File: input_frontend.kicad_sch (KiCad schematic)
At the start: 15 parts

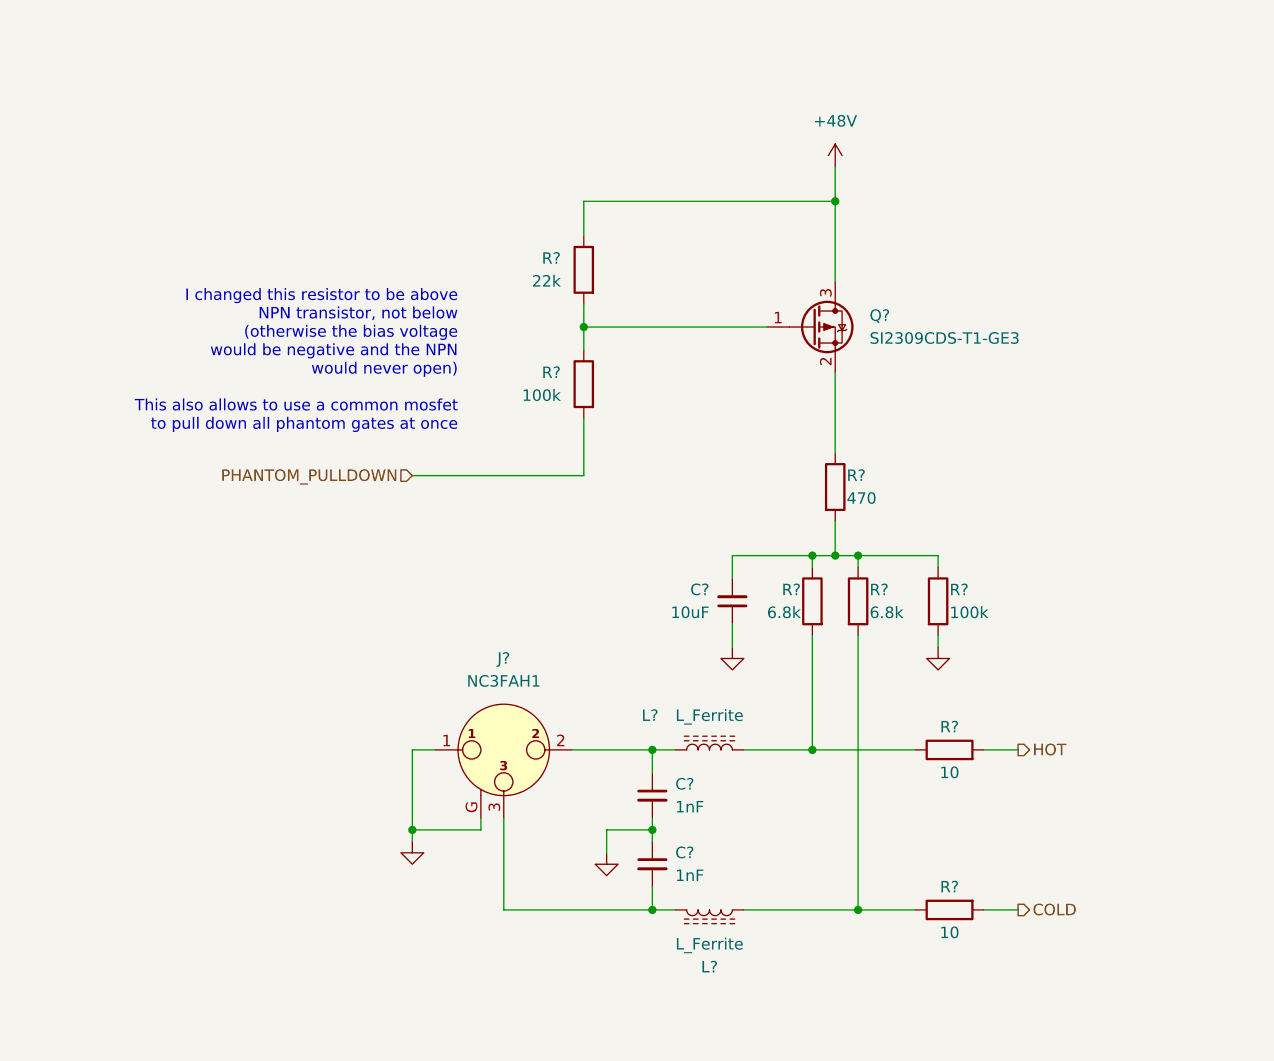
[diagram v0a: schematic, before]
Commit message: independent phantom control and removed transformer bias
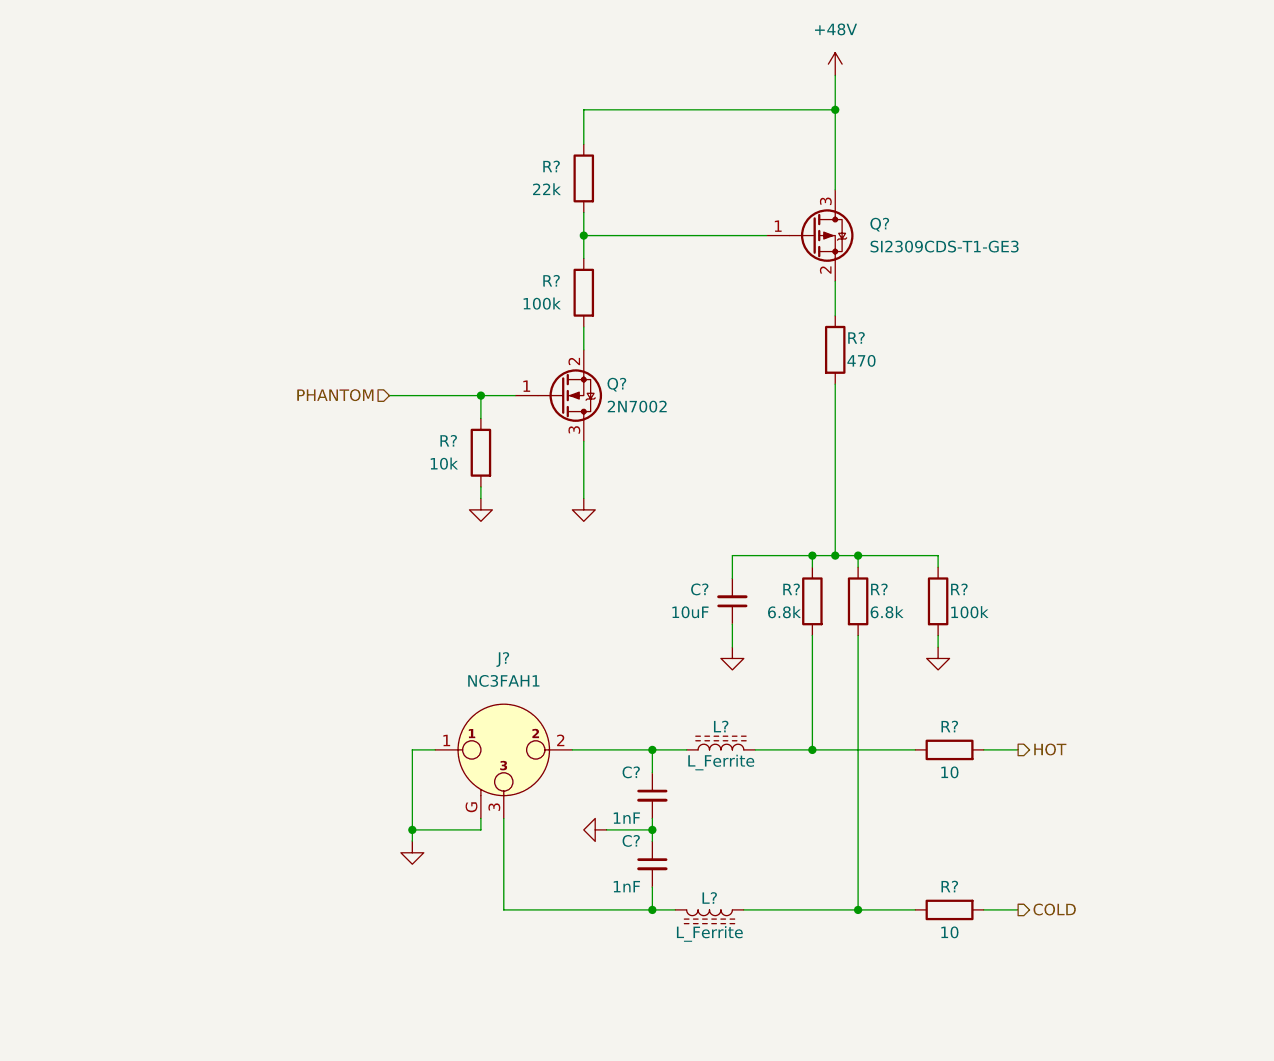
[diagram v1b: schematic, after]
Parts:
- added Q?: 2N7002, Package_TO_SOT_SMD:SOT-23, symbol Transistor_FET:2N7002
- added R?: 10k, Resistor_SMD:R_0603_1608Metric, symbol Device:R
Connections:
- net GND: now also Q?.3 (D), R?.2
- net PHANTOM_PULLDOWN: no longer names the net of R?.2
- net PHANTOM_PULLDOWN: now also Q?.2 (S)
- new net PHANTOM: Q?.1 (G), R?.1
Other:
- note removed: "I changed this resistor to be above NPN transistor, not below (otherwise the bias voltage would be negative and the NPN would never open) This also allows to use a common mosfet to pull down all phantom gates at once"
- moved on the sheet: L?, Q?, R?

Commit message: assign some component data
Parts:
- C16, C17: renamed from C?; value 1nF -> 1nF 63V; MPN (none) -> C 1nF 63V 0805
- C18: renamed from C?; MPN (none) -> C 10μF 16V 0805
- J2: renamed from J?; MPN (none) -> NC3FAH1
- L1, L2: renamed from L?; MPN (none) -> must select ferrite; now left out of the parts list
- Q1: renamed from Q?; MPN (none) -> 2N7002
- Q2: renamed from Q?; MPN (none) -> SI2309CDS-T1-GE3
- R10, R8: renamed from R?; MPN (none) -> R 6.8kΩ 125mW 1% 0805
- R11, R7: renamed from R?; MPN (none) -> R 100kΩ 125mW 5% 0805
- R12, R13: renamed from R?; MPN (none) -> R 10Ω 125mW 5% 0805
- R5: renamed from R?; MPN (none) -> R 10kΩ 125mW 5% 0805
- R6: renamed from R?; MPN (none) -> R 22kΩ 125mW 5% 0805
- R9: renamed from R?; MPN (none) -> R 470Ω 125mW 5% 0805

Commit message: some final touches
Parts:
- added R14: 13kΩ, Resistor_SMD:R_0603_1608Metric, symbol Device:R
- R10, R8: value 6.8k -> 6.8kΩ
- R11, R7: value 100k -> 100kΩ
- R12, R13: value 10 -> 2.2kΩ; MPN R 10Ω 125mW 5% 0805 -> R 2.2kΩ 125mW 1% 0805
- R5: value 10k -> 10kΩ
- R6: value 22k -> 22kΩ
- R9: value 470 -> 470Ω
- renumbered J2 to J1
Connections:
- net COLD: now also R14.2
- net HOT: now also R14.1
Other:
- note added: "replace with 10Ω and remove parallel resistor to disable pad"
- note added: "≈6dB pad with ≈10k impedance"

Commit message: update component assignments
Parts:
- C16, C17: MPN C 1nF 63V 0805 -> C 1nF 63V 0603
- C18: footprint Capacitor_SMD:C_0603_1608Metric -> Capacitor_SMD:C_0805_2012Metric
- R10, R8: MPN R 6.8kΩ 125mW 1% 0805 -> R 6.8kΩ 125mW 1% 0603
- R11, R7: MPN R 100kΩ 125mW 5% 0805 -> R 100kΩ 125mW 5% 0603
- R12, R13: MPN R 2.2kΩ 125mW 1% 0805 -> R 2.2kΩ 125mW 1% 0603
- R14: MPN R 13kΩ 125mW 1% 0805 -> R 13kΩ 125mW 1% 0603
- R5: MPN R 10kΩ 125mW 5% 0805 -> R 10kΩ 125mW 5% 0603
- R6: MPN R 22kΩ 125mW 5% 0805 -> R 22kΩ 125mW 5% 0603
- R9: MPN R 470Ω 125mW 5% 0805 -> R 470Ω 125mW 5% 0603
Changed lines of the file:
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@@
 			)
 		)
-		(property "MPN" "R 2.2kΩ 125mW 1% 0805"
+		(property "MPN" "R 2.2kΩ 125mW 1% 0603"
 			(at 156.21 129.54 90)
 			(effects
@@
 			)
 		)
-		(property "MPN" "R 2.2kΩ 125mW 1% 0805"
+		(property "MPN" "R 2.2kΩ 125mW 1% 0603"
 			(at 156.21 111.76 90)
 			(effects
@@
 			)
 		)
-		(property "MPN" "C 1nF 63V 0805"
+		(property "MPN" "C 1nF 63V 0603"
 			(at 123.19 116.84 0)
 			(effects
@@
 			)
 		)
-		(property "MPN" "R 6.8kΩ 125mW 1% 0805"
+		(property "MPN" "R 6.8kΩ 125mW 1% 0603"
 			(at 140.97 95.25 0)
 			(effects
@@
 			)
 		)
-		(property "MPN" "R 6.8kΩ 125mW 1% 0805"
+		(property "MPN" "R 6.8kΩ 125mW 1% 0603"
 			(at 146.05 95.25 0)
 			(effects
@@
 			)
 		)
-		(property "MPN" "R 100kΩ 125mW 5% 0805"
+		(property "MPN" "R 100kΩ 125mW 5% 0603"
 			(at 115.57 60.96 0)
 			(effects
@@
 			)
 		)
-		(property "MPN" "R 470Ω 125mW 5% 0805"
+		(property "MPN" "R 470Ω 125mW 5% 0603"
 			(at 143.51 67.31 0)
 			(effects
@@
 			)
 		)
-		(property "MPN" "R 100kΩ 125mW 5% 0805"
+		(property "MPN" "R 100kΩ 125mW 5% 0603"
 			(at 154.94 95.25 0)
 			(effects
@@
 			)
 		)
-		(property "MPN" "R 13kΩ 125mW 1% 0805"
+		(property "MPN" "R 13kΩ 125mW 1% 0603"
 			(at 166.37 120.65 0)
 			(effects
@@
 			)
 		)
-		(property "MPN" "R 22kΩ 125mW 5% 0805"
+		(property "MPN" "R 22kΩ 125mW 5% 0603"
 			(at 115.57 48.26 0)
 			(effects
@@
 			)
 		)
-		(property "MPN" "C 1nF 63V 0805"
+		(property "MPN" "C 1nF 63V 0603"
 			(at 123.19 124.46 0)
 			(effects
@@
 			)
 		)
-		(property "Footprint" "Capacitor_SMD:C_0603_1608Metric"
+		(property "Footprint" "Capacitor_SMD:C_0805_2012Metric"
 			(at 132.08 95.25 0)
 			(effects
@@
 			)
 		)
-		(property "MPN" "R 10kΩ 125mW 5% 0805"
+		(property "MPN" "R 10kΩ 125mW 5% 0603"
 			(at 104.14 78.74 0)
 			(effects

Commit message: sync pcb
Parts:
- C22: renamed from C18; value 10uF -> 10μF
- L1, L2: value L_Ferrite -> 10μH 15mA; footprint (none) -> Inductor_SMD:L_0805_2012Metric; LCSC (none) -> C1046; MPN must select ferrite -> SDFL1608S100KTF or LQM21FN100N00L
- renumbered C16 to C20, C17 to C21
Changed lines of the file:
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@@
 		(on_board yes)
 		(dnp no)
-		(property "Reference" "C16"
+		(property "Reference" "C20"
 			(at 121.92 114.3 0)
 			(effects
@@
 			(project "mv2_taa3040"
 				(path "/41a55a1d-5108-482f-b313-9eaa5d011dff/1c3f6b07-c9aa-4f11-804b-09faf49e24ef/b6e2052b-48ff-4d09-8780-3157be176bf9"
-					(reference "C22")
-					(unit 1)
-				)
-				(path "/41a55a1d-5108-482f-b313-9eaa5d011dff/bd2f1d91-73ea-4344-9315-80da99bbdd84/b6e2052b-48ff-4d09-8780-3157be176bf9"
-					(reference "C16")
-					(unit 1)
-				)
-				(path "/41a55a1d-5108-482f-b313-9eaa5d011dff/e3f94415-cffd-4131-bc0e-4234c6300c0c/3bf1189a-5745-484e-b713-f473b34ebbfc"
-					(reference "C27")
-					(unit 1)
-				)
-				(path "/41a55a1d-5108-482f-b313-9eaa5d011dff/ec88f180-6d4b-439f-8697-a1ff92f435a7/3bf1189a-5745-484e-b713-f473b34ebbfc"
-					(reference "C19")
+					(reference "C26")
+					(unit 1)
+				)
+				(path "/41a55a1d-5108-482f-b313-9eaa5d011dff/bd2f1d91-73ea-4344-9315-80da99bbdd84/b6e2052b-48ff-4d09-8780-3157be176bf9"
+					(reference "C20")
+					(unit 1)
+				)
+				(path "/41a55a1d-5108-482f-b313-9eaa5d011dff/e3f94415-cffd-4131-bc0e-4234c6300c0c/3bf1189a-5745-484e-b713-f473b34ebbfc"
+					(reference "C31")
+					(unit 1)
+				)
+				(path "/41a55a1d-5108-482f-b313-9eaa5d011dff/ec88f180-6d4b-439f-8697-a1ff92f435a7/3bf1189a-5745-484e-b713-f473b34ebbfc"
+					(reference "C23")
 					(unit 1)
 				)
@@
 			)
 		)
-		(property "Value" "L_Ferrite"
+		(property "Value" "10μH 15mA"
 			(at 129.54 132.08 90)
 			(effects
@@
 			)
 		)
-		(property "Footprint" ""
+		(property "Footprint" "Inductor_SMD:L_0805_2012Metric"
 			(at 129.54 129.54 0)
 			(effects
@@
 			)
 		)
-		(property "MPN" "must select ferrite"
+		(property "MPN" "SDFL1608S100KTF or LQM21FN100N00L"
+			(at 129.54 129.54 90)
+			(effects
+				(font
+					(size 1.27 1.27)
+				)
+				(hide yes)
+			)
+		)
+		(property "LCSC" "C1046"
 			(at 129.54 129.54 90)
 			(effects
@@
 			)
 		)
-		(property "Value" "L_Ferrite"
+		(property "Value" "10μH 15mA"
 			(at 130.81 113.03 90)
 			(effects
@@
 			)
 		)
-		(property "Footprint" ""
+		(property "Footprint" "Inductor_SMD:L_0805_2012Metric"
 			(at 130.81 111.76 0)
 			(effects
@@
 			)
 		)
-		(property "MPN" "must select ferrite"
+		(property "MPN" "SDFL1608S100KTF or LQM21FN100N00L"
+			(at 130.81 111.76 90)
+			(effects
+				(font
+					(size 1.27 1.27)
+				)
+				(hide yes)
+			)
+		)
+		(property "LCSC" "C1046"
 			(at 130.81 111.76 90)
 			(effects
@@
 		(on_board yes)
 		(dnp no)
-		(property "Reference" "C17"
+		(property "Reference" "C21"
 			(at 121.92 121.92 0)
 			(effects
@@
 			(project "mv2_taa3040"
 				(path "/41a55a1d-5108-482f-b313-9eaa5d011dff/1c3f6b07-c9aa-4f11-804b-09faf49e24ef/b6e2052b-48ff-4d09-8780-3157be176bf9"
-					(reference "C23")
-					(unit 1)
-				)
-				(path "/41a55a1d-5108-482f-b313-9eaa5d011dff/bd2f1d91-73ea-4344-9315-80da99bbdd84/b6e2052b-48ff-4d09-8780-3157be176bf9"
-					(reference "C17")
-					(unit 1)
-				)
-				(path "/41a55a1d-5108-482f-b313-9eaa5d011dff/e3f94415-cffd-4131-bc0e-4234c6300c0c/3bf1189a-5745-484e-b713-f473b34ebbfc"
-					(reference "C28")
-					(unit 1)
-				)
-				(path "/41a55a1d-5108-482f-b313-9eaa5d011dff/ec88f180-6d4b-439f-8697-a1ff92f435a7/3bf1189a-5745-484e-b713-f473b34ebbfc"
-					(reference "C20")
+					(reference "C27")
+					(unit 1)
+				)
+				(path "/41a55a1d-5108-482f-b313-9eaa5d011dff/bd2f1d91-73ea-4344-9315-80da99bbdd84/b6e2052b-48ff-4d09-8780-3157be176bf9"
+					(reference "C21")
+					(unit 1)
+				)
+				(path "/41a55a1d-5108-482f-b313-9eaa5d011dff/e3f94415-cffd-4131-bc0e-4234c6300c0c/3bf1189a-5745-484e-b713-f473b34ebbfc"
+					(reference "C32")
+					(unit 1)
+				)
+				(path "/41a55a1d-5108-482f-b313-9eaa5d011dff/ec88f180-6d4b-439f-8697-a1ff92f435a7/3bf1189a-5745-484e-b713-f473b34ebbfc"
+					(reference "C24")
 					(unit 1)
 				)
@@
 		(on_board yes)
 		(dnp no)
-		(property "Reference" "C18"
+		(property "Reference" "C22"
 			(at 129.54 93.9735 0)
 			(effects
@@
 			)
 		)
-		(property "Value" "10uF"
+		(property "Value" "10μF"
 			(at 129.54 96.5135 0)
 			(effects
@@
 			(project "mv2_taa3040"
 				(path "/41a55a1d-5108-482f-b313-9eaa5d011dff/1c3f6b07-c9aa-4f11-804b-09faf49e24ef/b6e2052b-48ff-4d09-8780-3157be176bf9"
-					(reference "C24")
-					(unit 1)
-				)
-				(path "/41a55a1d-5108-482f-b313-9eaa5d011dff/bd2f1d91-73ea-4344-9315-80da99bbdd84/b6e2052b-48ff-4d09-8780-3157be176bf9"
-					(reference "C18")
-					(unit 1)
-				)
-				(path "/41a55a1d-5108-482f-b313-9eaa5d011dff/e3f94415-cffd-4131-bc0e-4234c6300c0c/3bf1189a-5745-484e-b713-f473b34ebbfc"
-					(reference "C29")
-					(unit 1)
-				)
-				(path "/41a55a1d-5108-482f-b313-9eaa5d011dff/ec88f180-6d4b-439f-8697-a1ff92f435a7/3bf1189a-5745-484e-b713-f473b34ebbfc"
-					(reference "C21")
-					(unit 1)
-				)
+					(reference "C28")
+					(unit 1)
+				)
+				(path "/41a55a1d-5108-482f-b313-9eaa5d011dff/bd2f1d91-73ea-4344-9315-80da99bbdd84/b6e2052b-48ff-4d09-8780-3157be176bf9"
+					(reference "C22")
+					(unit 1)
+				)
+				(path "/41a55a1d-5108-482f-b313-9eaa5d011dff/e3f94415-cffd-4131-bc0e-4234c6300c0c/3bf1189a-5745-484e-b713-f473b34ebbfc"
+					(reference "C33")
+					(unit 1)
+				)
+				(path "/41a55a1d-5108-482f-b313-9eaa5d011dff/ec88f180-6d4b-439f-8697-a1ff92f435a7/3bf1189a-5745-484e-b713-f473b34ebbfc"
+					(reference "C25")
+					(unit 1)
+				)
